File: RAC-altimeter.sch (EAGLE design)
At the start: 24 parts, among them IC1 RN4871-I_RM130, J1 MICRO-SD, U1 MAX32660GTP+, U2 BMI088, U3 BMP388, U4 TPS73733DCQR, Y1 32.768kHz

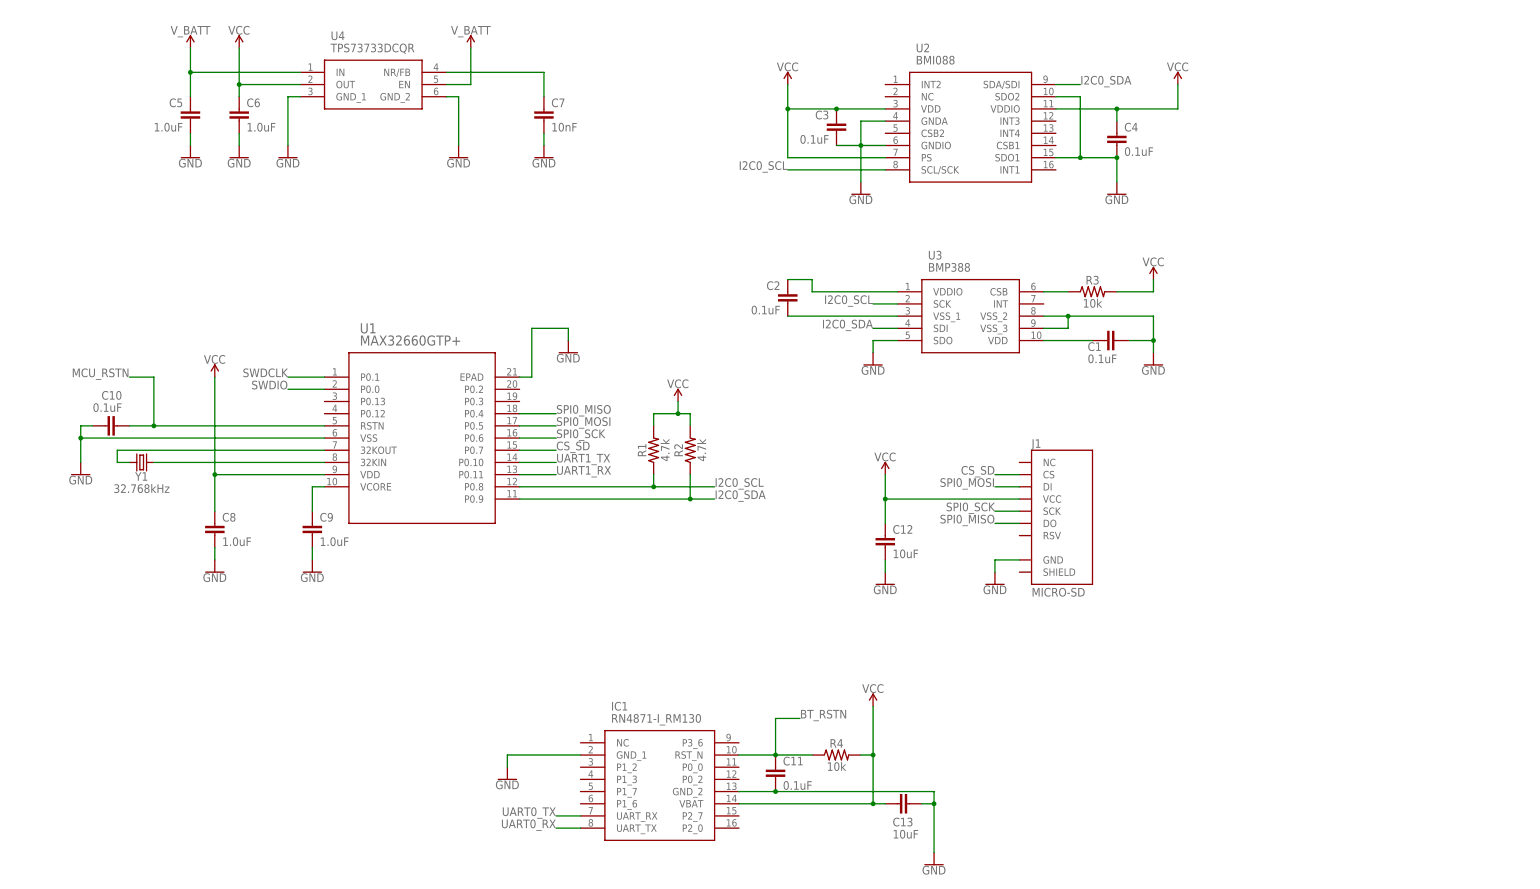
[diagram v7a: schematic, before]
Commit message: Replaced the LDO with a TPS62172 buck converter
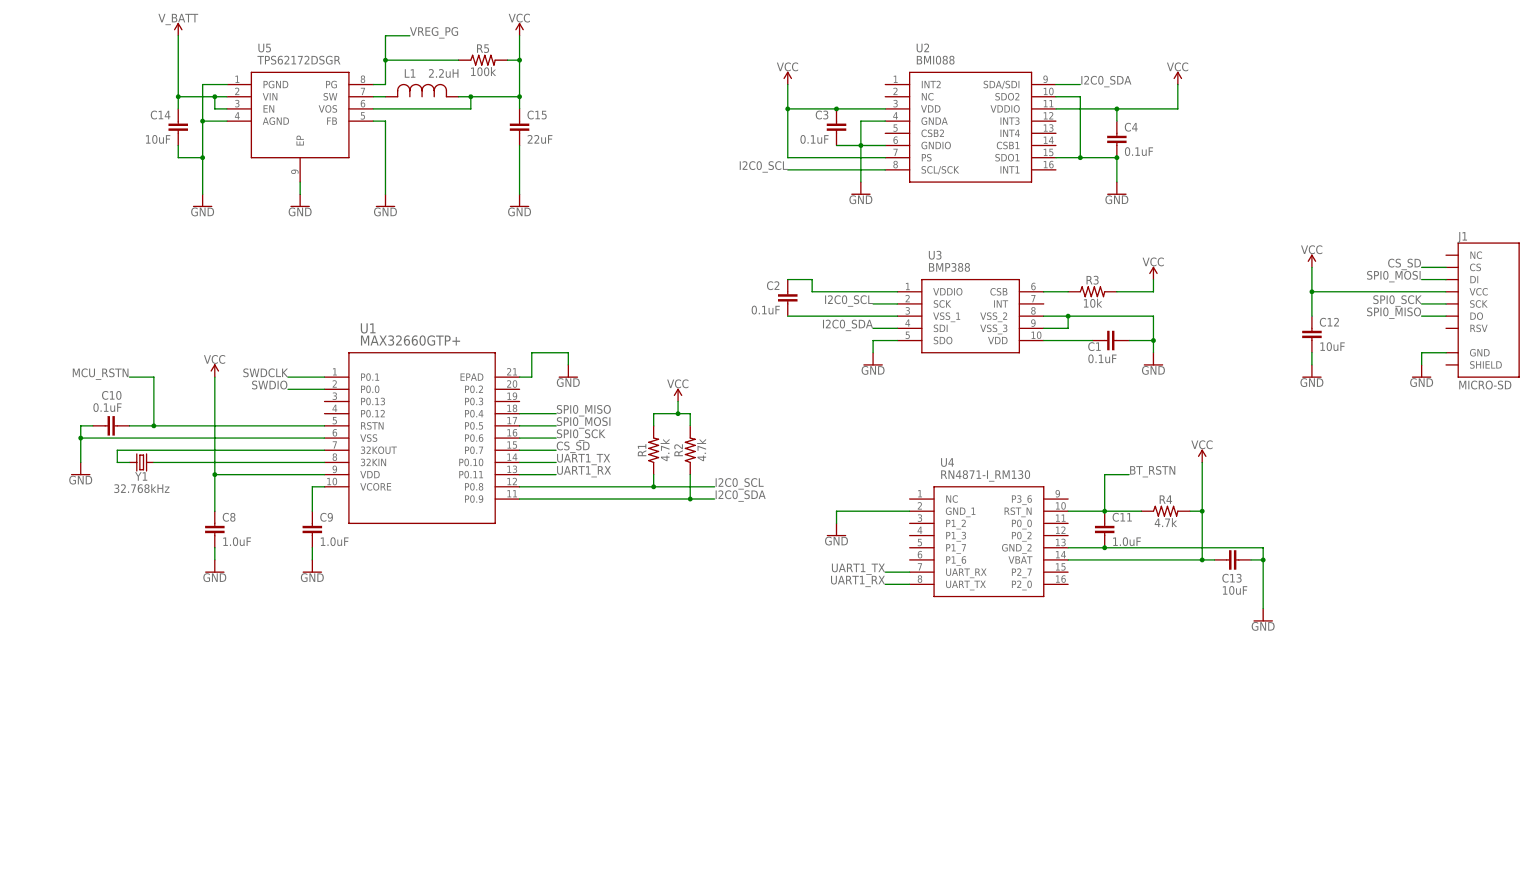
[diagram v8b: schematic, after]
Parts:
- removed C5, C6: 1.0uF, SparkFun-Capacitors:1.0UF-0603-16V-10%
- removed C7: 10nF, SparkFun-Capacitors:10NF-0603-50V-10%
- removed IC1: RN4871-I_RM130, RAC-Altimeter:RN4871-I_RM130
- added C14: 10uF, SparkFun-Capacitors:10UF-0603-6.3V-20%
- added C15: 22uF, SparkFun-Capacitors:22UF-0805-6.3V-20%
- added L1: 2.2uH, RAC-Altimeter:MAMK2520T2R2M
- added R5: 100k, SparkFun-Resistors:100KOHM-0603-1/10W-1%
- added U5: TPS62172DSGR, RAC-Altimeter:TPS62172DSGR
- C11: value 0.1uF -> 1.0uF; device SparkFun-Capacitors:0.1UF-0603-25V-(+80/-20%) -> SparkFun-Capacitors:1.0UF-0603-16V-10%
- R4: value 10k -> 4.7k; device SparkFun-Resistors:10KOHM-0603-1/10W-1% -> SparkFun-Resistors:4.7KOHM-0603-1/10W-1%
- U4: value TPS73733DCQR -> RN4871-I_RM130; device RAC-Altimeter:TPS73733DCQR -> RAC-Altimeter:RN4871-I_RM130
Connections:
- removed net N$8: C7.1, U4.NR/FB
- removed net UART0_RX: IC1.UART_TX
- removed net UART0_TX: IC1.UART_RX
- new net N$1: L1.2, U5.SW
- new net VREG_PG: R5.1, U5.PG
- net BT_RSTN: now also U4.RST_N; no longer IC1.RST_N
- net GND: now also C14.2, C15.2, U5.AGND, U5.EP, U5.FB, U5.PGND; no longer C5.2, C6.2, C7.2, IC1.GND_1, IC1.GND_2
- net UART1_RX: now also U4.UART_TX
- net UART1_TX: now also U4.UART_RX
- net VCC: now also C15.1, L1.1, R5.2, U4.VBAT, U5.VOS; no longer C6.1, IC1.VBAT, U4.OUT
- net V_BATT: now also C14.1, U5.EN, U5.VIN; no longer C5.1, U4.EN, U4.IN
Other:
- moved on the sheet: C11, C12, C13, J1, R4
